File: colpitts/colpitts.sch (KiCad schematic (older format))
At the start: 37 parts, among them J101 BORNERA, J102 BNC, Q101 2N3904, Q102 2N3904, Q103 2N3904, Q104 2N3904, U101 LM741

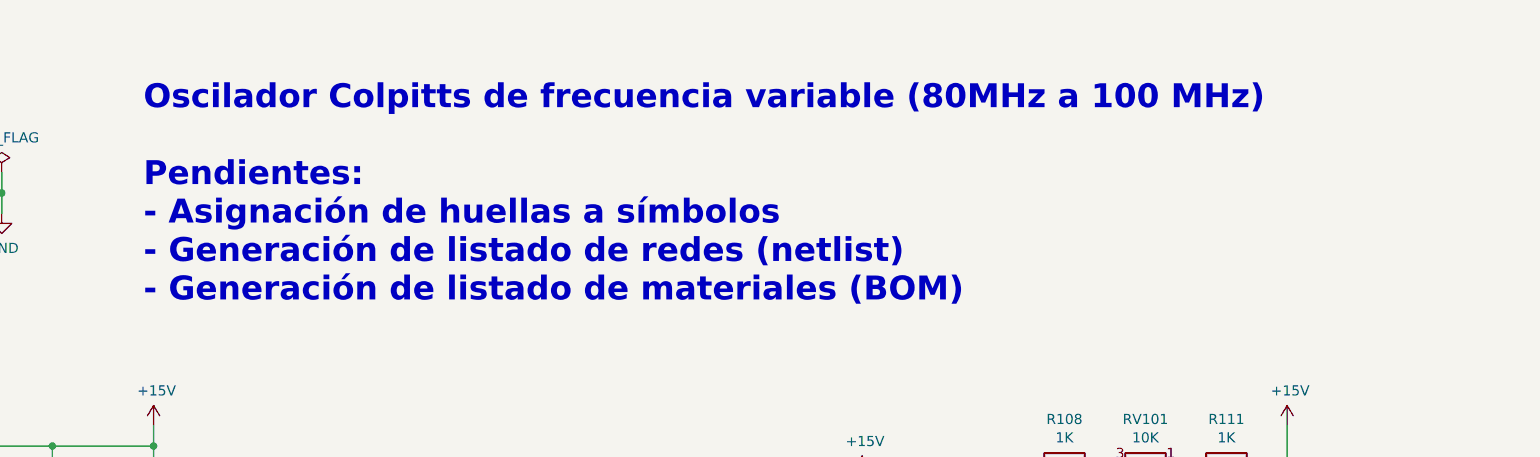
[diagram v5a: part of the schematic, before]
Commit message: Update diseño esquemático (asignación de huellas y modelos 3d)
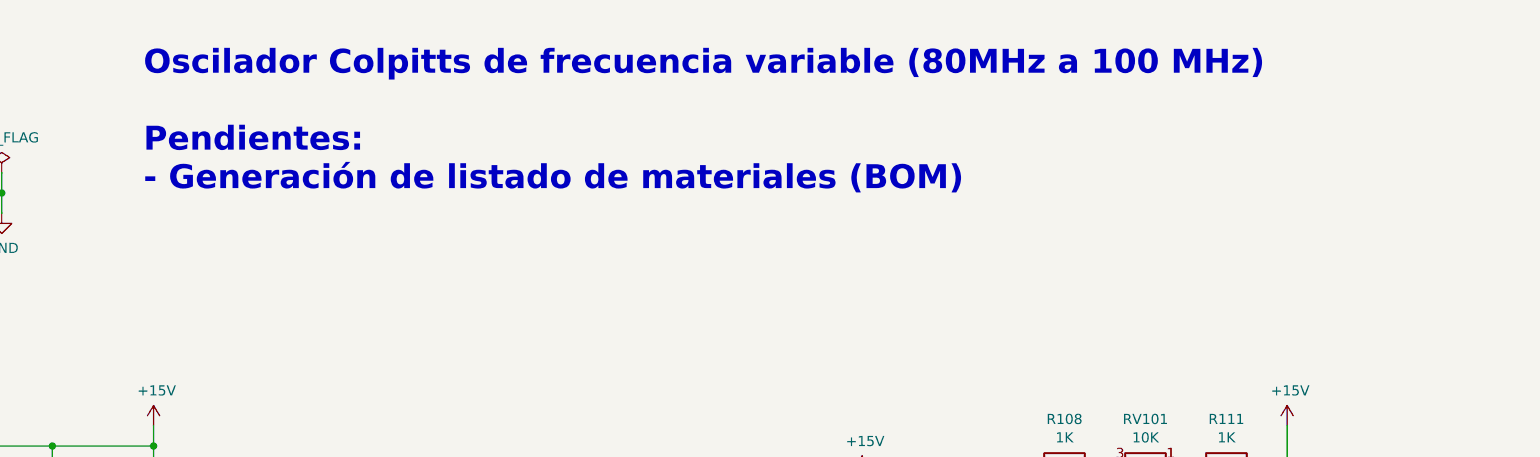
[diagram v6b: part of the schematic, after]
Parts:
- C101, C102, C103, C104, C105, C106, C107, C108, C110, C111, C112, C113, C114, C115: footprint (none) -> Capacitor_SMD:C_0805_2012Metric_Pad1.15x1.40mm_HandSolder
- C109: footprint (none) -> colpitts:Trimmer_Capacitor_Verde
- J101: footprint (none) -> colpitts:TerminalBlock_1x04_P5.00mm
- J102: footprint (none) -> colpitts:BNC_Conn_Horizontal
- JP101, JP102: footprint (none) -> Connector_PinHeader_2.54mm:PinHeader_1x02_P2.54mm_Vertical
- L101: footprint (none) -> Inductor_THT:L_Axial_L5.3mm_D2.2mm_P10.16mm_Horizontal_Vishay_IM-1
- R101, R102, R103, R104, R105, R106, R107, R108, R109, R110, R111: footprint (none) -> Resistor_SMD:R_0805_2012Metric_Pad1.15x1.40mm_HandSolder
- RV101: footprint (none) -> colpitts:Preset_Multivuelta
- U101: footprint (none) -> Package_DIP:DIP-8_W10.16mm
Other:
- note added: "Oscilador Colpitts de frecuencia variable (80MHz a 100 MHz)\n\nPendientes:\n- Generación de listado de materiales (BOM)"
- note removed: "Oscilador Colpitts de frecuencia variable (80MHz a 100 MHz)\n\nPendientes:\n- Asignación de huellas a símbolos\n- Generación de listado de redes (netlist)\n- Generación de listado de materiales (BOM)"
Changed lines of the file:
@@
 F 0 "C101" H 2115 3146 50  0000 L CNN
 F 1 "1nF" H 2115 3055 50  0000 L CNN
-F 2 "" H 2038 2950 50  0001 C CNN
+F 2 "Capacitor_SMD:C_0805_2012Metric_Pad1.15x1.40mm_HandSolder" H 2038 2950 50  0001 C CNN
 F 3 "~" H 2000 3100 50  0001 C CNN
 	1    2000 3100
@@
 F 0 "C103" H 2615 3146 50  0000 L CNN
 F 1 "10nF" H 2615 3055 50  0000 L CNN
-F 2 "" H 2538 2950 50  0001 C CNN
+F 2 "Capacitor_SMD:C_0805_2012Metric_Pad1.15x1.40mm_HandSolder" H 2538 2950 50  0001 C CNN
 F 3 "~" H 2500 3100 50  0001 C CNN
 	1    2500 3100
@@
 F 0 "C105" H 3115 3146 50  0000 L CNN
 F 1 "100nF" H 3115 3055 50  0000 L CNN
-F 2 "" H 3038 2950 50  0001 C CNN
+F 2 "Capacitor_SMD:C_0805_2012Metric_Pad1.15x1.40mm_HandSolder" H 3038 2950 50  0001 C CNN
 F 3 "~" H 3000 3100 50  0001 C CNN
 	1    3000 3100
@@
 F 0 "R102" H 3570 3146 50  0000 L CNN
 F 1 "10K" H 3570 3055 50  0000 L CNN
-F 2 "" V 3430 3100 50  0001 C CNN
+F 2 "Resistor_SMD:R_0805_2012Metric_Pad1.15x1.40mm_HandSolder" V 3430 3100 50  0001 C CNN
 F 3 "~" H 3500 3100 50  0001 C CNN
 	1    3500 3100
@@
 F 0 "L101" H 4053 3146 50  0000 L CNN
 F 1 "40n" H 4053 3055 50  0000 L CNN
-F 2 "" H 4000 3100 50  0001 C CNN
+F 2 "Inductor_THT:L_Axial_L5.3mm_D2.2mm_P10.16mm_Horizontal_Vishay_IM-1" H 4000 3100 50  0001 C CNN
 F 3 "~" H 4000 3100 50  0001 C CNN
 	1    4000 3100
@@
 F 0 "R103" H 3570 4246 50  0000 L CNN
 F 1 "10K" H 3570 4155 50  0000 L CNN
-F 2 "" V 3430 4200 50  0001 C CNN
+F 2 "Resistor_SMD:R_0805_2012Metric_Pad1.15x1.40mm_HandSolder" V 3430 4200 50  0001 C CNN
 F 3 "~" H 3500 4200 50  0001 C CNN
 	1    3500 4200
@@
 F 0 "C102" H 2115 4246 50  0000 L CNN
 F 1 "1nF" H 2115 4155 50  0000 L CNN
-F 2 "" H 2038 4050 50  0001 C CNN
+F 2 "Capacitor_SMD:C_0805_2012Metric_Pad1.15x1.40mm_HandSolder" H 2038 4050 50  0001 C CNN
 F 3 "~" H 2000 4200 50  0001 C CNN
 	1    2000 4200
@@
 F 0 "C104" H 2615 4246 50  0000 L CNN
 F 1 "10nF" H 2615 4155 50  0000 L CNN
-F 2 "" H 2538 4050 50  0001 C CNN
+F 2 "Capacitor_SMD:C_0805_2012Metric_Pad1.15x1.40mm_HandSolder" H 2538 4050 50  0001 C CNN
 F 3 "~" H 2500 4200 50  0001 C CNN
 	1    2500 4200
@@
 F 0 "C106" H 3115 4246 50  0000 L CNN
 F 1 "100nF" H 3115 4155 50  0000 L CNN
-F 2 "" H 3038 4050 50  0001 C CNN
+F 2 "Capacitor_SMD:C_0805_2012Metric_Pad1.15x1.40mm_HandSolder" H 3038 4050 50  0001 C CNN
 F 3 "~" H 3000 4200 50  0001 C CNN
 	1    3000 4200
@@
 F 0 "R105" H 3930 5404 50  0000 R CNN
 F 1 "330" H 3930 5495 50  0000 R CNN
-F 2 "" V 3930 5450 50  0001 C CNN
+F 2 "Resistor_SMD:R_0805_2012Metric_Pad1.15x1.40mm_HandSolder" V 3930 5450 50  0001 C CNN
 F 3 "~" H 4000 5450 50  0001 C CNN
 	1    4000 5450
@@
 F 0 "R104" V 3957 5950 50  0000 C CNN
 F 1 "330" V 3866 5950 50  0000 C CNN
-F 2 "" V 3680 5950 50  0001 C CNN
+F 2 "Resistor_SMD:R_0805_2012Metric_Pad1.15x1.40mm_HandSolder" V 3680 5950 50  0001 C CNN
 F 3 "~" H 3750 5950 50  0001 C CNN
 	1    3750 5950
@@
 F 0 "R101" V 2957 4950 50  0000 C CNN
 F 1 "3.9K" V 2866 4950 50  0000 C CNN
-F 2 "" V 2680 4950 50  0001 C CNN
+F 2 "Resistor_SMD:R_0805_2012Metric_Pad1.15x1.40mm_HandSolder" V 2680 4950 50  0001 C CNN
 F 3 "~" H 2750 4950 50  0001 C CNN
 	1    2750 4950
@@
 F 0 "C107" H 4615 3996 50  0000 L CNN
 F 1 "15pF" H 4615 3905 50  0000 L CNN
-F 2 "" H 4538 3800 50  0001 C CNN
+F 2 "Capacitor_SMD:C_0805_2012Metric_Pad1.15x1.40mm_HandSolder" H 4538 3800 50  0001 C CNN
 F 3 "~" H 4500 3950 50  0001 C CNN
 	1    4500 3950
@@
 F 0 "C108" H 4615 4496 50  0000 L CNN
 F 1 "68pF" H 4615 4405 50  0000 L CNN
-F 2 "" H 4538 4300 50  0001 C CNN
+F 2 "Capacitor_SMD:C_0805_2012Metric_Pad1.15x1.40mm_HandSolder" H 4538 4300 50  0001 C CNN
 F 3 "~" H 4500 4450 50  0001 C CNN
 	1    4500 4450
@@
 F 0 "C109" H 5125 3950 50  0000 L CNN
 F 1 "TRIM VERDE (5.2pF-30pF)" H 4525 4575 50  0000 L CNN
-F 2 "" H 5000 3950 50  0001 C CNN
+F 2 "colpitts:Trimmer_Capacitor_Verde" H 5000 3950 50  0001 C CNN
 F 3 "~" H 5000 3950 50  0001 C CNN
 	1    5000 3950
@@
 F 0 "C110" H 5615 3996 50  0000 L CNN
 F 1 "10pF" H 5615 3905 50  0000 L CNN
-F 2 "" H 5538 3800 50  0001 C CNN
+F 2 "Capacitor_SMD:C_0805_2012Metric_Pad1.15x1.40mm_HandSolder" H 5538 3800 50  0001 C CNN
 F 3 "~" H 5500 3950 50  0001 C CNN
 	1    5500 3950
@@
 F 0 "C111" H 5615 4496 50  0000 L CNN
 F 1 "33pF" H 5615 4405 50  0000 L CNN
-F 2 "" H 5538 4300 50  0001 C CNN
+F 2 "Capacitor_SMD:C_0805_2012Metric_Pad1.15x1.40mm_HandSolder" H 5538 4300 50  0001 C CNN
 F 3 "~" H 5500 4450 50  0001 C CNN
 	1    5500 4450
@@
 F 0 "C112" V 5748 3500 50  0000 C CNN
 F 1 "100nF" V 5839 3500 50  0000 C CNN
-F 2 "" H 6038 3350 50  0001 C CNN
+F 2 "Capacitor_SMD:C_0805_2012Metric_Pad1.15x1.40mm_HandSolder" H 6038 3350 50  0001 C CNN
 F 3 "~" H 6000 3500 50  0001 C CNN
 	1    6000 3500
@@
 F 0 "J102" H 6350 4225 50  0000 L CNN
 F 1 "BNC" H 6350 4134 50  0000 L CNN
-F 2 "" H 6250 4250 50  0001 C CNN
+F 2 "colpitts:BNC_Conn_Horizontal" H 6250 4250 50  0001 C CNN
 F 3 " ~" H 6250 4250 50  0001 C CNN
 	1    6250 4250
@@
 F 0 "JP101" H 2250 5093 50  0000 C CNN
 F 1 "Jumper_2_Open" H 2250 5094 50  0001 C CNN
-F 2 "" H 2250 4950 50  0001 C CNN
+F 2 "Connector_PinHeader_2.54mm:PinHeader_1x02_P2.54mm_Vertical" H 2250 4950 50  0001 C CNN
 F 3 "~" H 2250 4950 50  0001 C CNN
 	1    2250 4950
@@
 F 0 "JP102" H 6500 3643 50  0000 C CNN
 F 1 "Jumper_2_Open" H 6500 3644 50  0001 C CNN
-F 2 "" H 6500 3500 50  0001 C CNN
+F 2 "Connector_PinHeader_2.54mm:PinHeader_1x02_P2.54mm_Vertical" H 6500 3500 50  0001 C CNN
 F 3 "~" H 6500 3500 50  0001 C CNN
 	1    6500 3500
@@
 F 0 "R106" H 6930 4054 50  0000 R CNN
 F 1 "10K" H 6930 4145 50  0000 R CNN
-F 2 "" V 6930 4100 50  0001 C CNN
+F 2 "Resistor_SMD:R_0805_2012Metric_Pad1.15x1.40mm_HandSolder" V 6930 4100 50  0001 C CNN
 F 3 "~" H 7000 4100 50  0001 C CNN
 	1    7000 4100
@@
 F 0 "R107" H 7430 4054 50  0000 R CNN
 F 1 "5.6K" H 7430 4145 50  0000 R CNN
-F 2 "" V 7430 4100 50  0001 C CNN
+F 2 "Resistor_SMD:R_0805_2012Metric_Pad1.15x1.40mm_HandSolder" V 7430 4100 50  0001 C CNN
 F 3 "~" H 7500 4100 50  0001 C CNN
 	1    7500 4100
@@
 F 0 "C114" H 8725 4050 50  0000 C CNN
 F 1 "100pF" H 8650 4150 50  0000 C CNN
-F 2 "" H 8938 3950 50  0001 C CNN
+F 2 "Capacitor_SMD:C_0805_2012Metric_Pad1.15x1.40mm_HandSolder" H 8938 3950 50  0001 C CNN
 F 3 "~" H 8900 4100 50  0001 C CNN
 	1    8900 4100
@@
 F 0 "R110" H 8830 4454 50  0000 R CNN
 F 1 "1K" H 8830 4545 50  0000 R CNN
-F 2 "" V 8830 4500 50  0001 C CNN
+F 2 "Resistor_SMD:R_0805_2012Metric_Pad1.15x1.40mm_HandSolder" V 8830 4500 50  0001 C CNN
 F 3 "~" H 8900 4500 50  0001 C CNN
 	1    8900 4500
@@
 F 0 "RV101" V 8693 2925 50  0000 C CNN
 F 1 "10K" V 8784 2925 50  0000 C CNN
-F 2 "" H 8900 2925 50  0001 C CNN
+F 2 "colpitts:Preset_Multivuelta" H 8900 2925 50  0001 C CNN
 F 3 "~" H 8900 2925 50  0001 C CNN
 	1    8900 2925
@@
 F 0 "U101" H 9650 4000 50  0000 L CNN
 F 1 "LM741" H 9650 3900 50  0000 L CNN
-F 2 "" H 9750 3750 50  0001 C CNN
+F 2 "Package_DIP:DIP-8_W10.16mm" H 9750 3750 50  0001 C CNN
 F 3 "http://www.ti.com/lit/ds/symlink/lm741.pdf" H 9850 3850 50  0001 C CNN
 	1    9700 3700
@@
 F 0 "R108" V 8707 2925 50  0000 C CNN
 F 1 "1K" V 8616 2925 50  0000 C CNN
-F 2 "" V 8430 2925 50  0001 C CNN
+F 2 "Resistor_SMD:R_0805_2012Metric_Pad1.15x1.40mm_HandSolder" V 8430 2925 50  0001 C CNN
 F 3 "~" H 8500 2925 50  0001 C CNN
 	1    8500 2925
@@
 F 0 "R111" V 9507 2925 50  0000 C CNN
 F 1 "1K" V 9416 2925 50  0000 C CNN
-F 2 "" V 9230 2925 50  0001 C CNN
+F 2 "Resistor_SMD:R_0805_2012Metric_Pad1.15x1.40mm_HandSolder" V 9230 2925 50  0001 C CNN
 F 3 "~" H 9300 2925 50  0001 C CNN
 	1    9300 2925
@@
 F 0 "R109" V 8707 3800 50  0000 C CNN
 F 1 "1K" V 8616 3800 50  0000 C CNN
-F 2 "" V 8430 3800 50  0001 C CNN
+F 2 "Resistor_SMD:R_0805_2012Metric_Pad1.15x1.40mm_HandSolder" V 8430 3800 50  0001 C CNN
 F 3 "~" H 8500 3800 50  0001 C CNN
 	1    8500 3800
@@
 F 0 "C115" H 10215 3196 50  0000 L CNN
 F 1 "100nF" H 10215 3105 50  0000 L CNN
-F 2 "" H 10138 3000 50  0001 C CNN
+F 2 "Capacitor_SMD:C_0805_2012Metric_Pad1.15x1.40mm_HandSolder" H 10138 3000 50  0001 C CNN
 F 3 "~" H 10100 3150 50  0001 C CNN
 	1    10100 3150
@@
 F 0 "C113" H 7825 4050 50  0000 C CNN
 F 1 "10nF" H 7800 4150 50  0000 C CNN
-F 2 "" H 8038 3950 50  0001 C CNN
+F 2 "Capacitor_SMD:C_0805_2012Metric_Pad1.15x1.40mm_HandSolder" H 8038 3950 50  0001 C CNN
 F 3 "~" H 8000 4100 50  0001 C CNN
 	1    8000 4100
@@
 F 0 "J101" H 2450 1150 50  0000 C CNN
 F 1 "BORNERA" H 2450 1250 50  0000 C CNN
-F 2 "" H 2500 1600 50  0001 C CNN
+F 2 "colpitts:TerminalBlock_1x04_P5.00mm" H 2500 1600 50  0001 C CNN
 F 3 "~" H 2500 1600 50  0001 C CNN
 	1    2500 1600
@@
 	3250 1600 3250 1500
 Connection ~ 3250 1600
-Text Notes 3950 2150 0    118  ~ 24
-Oscilador Colpitts de frecuencia variable (80MHz a 100 MHz)\n\nPendientes:\n- Asignación de huellas a símbolos\n- Generación de listado de redes (netlist)\n- Generación de listado de materiales (BOM)
+Text Notes 3950 1600 0    118  ~ 24
+Oscilador Colpitts de frecuencia variable (80MHz a 100 MHz)\n\nPendientes:\n- Generación de listado de materiales (BOM)
 Text Label 1500 4950 0    50   ~ 0
 Vcontrol

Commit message: Fin diseño esquemático (bom generada)
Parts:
- C109: Description (none) -> CAP TRIMMER 5.2-30PF 100V TH; DigiKey PN (none) -> 490-1960-ND; Manf PN (none) -> TZ03R300E169B00
- J101: Description (none) -> TERM BLK 4POS SIDE ENTRY 5MM PCB; DigiKey PN (none) -> 277-1579-ND; Manf PN (none) -> 1935187
- J102: Description (none) -> CONN BNC JACK R/A 50 OHM PCB; DigiKey PN (none) -> A32244-ND; Manf PN (none) -> 5227161-1
- Q101, Q102, Q103, Q104: Description (none) -> TRANS NPN 40V 0.2A TO-92; DigiKey PN (none) -> 2N3904FS-ND; Manf PN (none) -> 2N3904BU
- U101: Description (none) -> IC OPAMP GP 1 CIRCUIT 8DIP; DigiKey PN (none) -> LM741CNNS/NOPB-ND; Manf PN (none) -> LM741CN/NOPB
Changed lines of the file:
@@
 F 1 "2N3904" H 4090 3905 50  0000 L CNN
 F 2 "Package_TO_SOT_THT:TO-92_Inline" H 4100 3875 50  0001 L CIN
-F 3 "https://www.fairchildsemi.com/datasheets/2N/2N3904.pdf" H 3900 3950 50  0001 L CNN
+F 3 "https://www.onsemi.com/pub/Collateral/PZT3904-D.pdf" H 3900 3950 50  0001 L CNN
+F 4 "TRANS NPN 40V 0.2A TO-92" H 3900 3950 50  0001 C CNN "Description"
+F 5 "2N3904FS-ND" H 3900 3950 50  0001 C CNN "DigiKey PN"
+F 6 "2N3904BU" H 3900 3950 50  0001 C CNN "Manf PN"
 	1    3900 3950
 	1    0    0    -1
@@
 F 1 "2N3904" H 4090 4905 50  0000 L CNN
 F 2 "Package_TO_SOT_THT:TO-92_Inline" H 4100 4875 50  0001 L CIN
-F 3 "https://www.fairchildsemi.com/datasheets/2N/2N3904.pdf" H 3900 4950 50  0001 L CNN
+F 3 "https://www.onsemi.com/pub/Collateral/PZT3904-D.pdf" H 3900 4950 50  0001 L CNN
+F 4 "TRANS NPN 40V 0.2A TO-92" H 3900 4950 50  0001 C CNN "Description"
+F 5 "2N3904FS-ND" H 3900 4950 50  0001 C CNN "DigiKey PN"
+F 6 "2N3904BU" H 3900 4950 50  0001 C CNN "Manf PN"
 	1    3900 4950
 	1    0    0    -1
@@
 F 1 "2N3904" H 3590 5405 50  0000 L CNN
 F 2 "Package_TO_SOT_THT:TO-92_Inline" H 3600 5375 50  0001 L CIN
-F 3 "https://www.fairchildsemi.com/datasheets/2N/2N3904.pdf" H 3400 5450 50  0001 L CNN
+F 3 "https://www.onsemi.com/pub/Collateral/PZT3904-D.pdf" H 3400 5450 50  0001 L CNN
+F 4 "TRANS NPN 40V 0.2A TO-92" H 3400 5450 50  0001 C CNN "Description"
+F 5 "2N3904FS-ND" H 3400 5450 50  0001 C CNN "DigiKey PN"
+F 6 "2N3904BU" H 3400 5450 50  0001 C CNN "Manf PN"
 	1    3400 5450
 	1    0    0    -1
@@
 F 1 "TRIM VERDE (5.2pF-30pF)" H 4525 4575 50  0000 L CNN
 F 2 "colpitts:Trimmer_Capacitor_Verde" H 5000 3950 50  0001 C CNN
-F 3 "~" H 5000 3950 50  0001 C CNN
+F 3 "https://media.digikey.com/pdf/Data%20Sheets/Murata%20PDFs/Ceramic_Trimmer_Cap_Cat.pdf#page=34" H 5000 3950 50  0001 C CNN
+F 4 "CAP TRIMMER 5.2-30PF 100V TH" H 5000 3950 50  0001 C CNN "Description"
+F 5 "490-1960-ND" H 5000 3950 50  0001 C CNN "DigiKey PN"
+F 6 "TZ03R300E169B00" H 5000 3950 50  0001 C CNN "Manf PN"
 	1    5000 3950
 	1    0    0    -1
@@
 F 1 "BNC" H 6350 4134 50  0000 L CNN
 F 2 "colpitts:BNC_Conn_Horizontal" H 6250 4250 50  0001 C CNN
-F 3 " ~" H 6250 4250 50  0001 C CNN
+F 3 "https://www.te.com/commerce/DocumentDelivery/DDEController?Action=srchrtrv&DocNm=5227161&DocType=Customer+Drawing&DocLang=English" H 6250 4250 50  0001 C CNN
+F 4 "CONN BNC JACK R/A 50 OHM PCB" H 6250 4250 50  0001 C CNN "Description"
+F 5 "A32244-ND" H 6250 4250 50  0001 C CNN "DigiKey PN"
+F 6 "5227161-1" H 6250 4250 50  0001 C CNN "Manf PN"
 	1    6250 4250
 	1    0    0    -1
@@
 F 1 "2N3904" H 7590 3455 50  0000 L CNN
 F 2 "Package_TO_SOT_THT:TO-92_Inline" H 7600 3425 50  0001 L CIN
-F 3 "https://www.fairchildsemi.com/datasheets/2N/2N3904.pdf" H 7400 3500 50  0001 L CNN
+F 3 "https://www.onsemi.com/pub/Collateral/PZT3904-D.pdf" H 7400 3500 50  0001 L CNN
+F 4 "TRANS NPN 40V 0.2A TO-92" H 7400 3500 50  0001 C CNN "Description"
+F 5 "2N3904FS-ND" H 7400 3500 50  0001 C CNN "DigiKey PN"
+F 6 "2N3904BU" H 7400 3500 50  0001 C CNN "Manf PN"
 	1    7400 3500
 	1    0    0    -1
@@
 F 2 "Package_DIP:DIP-8_W10.16mm" H 9750 3750 50  0001 C CNN
 F 3 "http://www.ti.com/lit/ds/symlink/lm741.pdf" H 9850 3850 50  0001 C CNN
+F 4 "IC OPAMP GP 1 CIRCUIT 8DIP" H 9700 3700 50  0001 C CNN "Description"
+F 5 "LM741CNNS/NOPB-ND" H 9700 3700 50  0001 C CNN "DigiKey PN"
+F 6 "LM741CN/NOPB" H 9700 3700 50  0001 C CNN "Manf PN"
 	1    9700 3700
 	1    0    0    -1
@@
 F 1 "BORNERA" H 2450 1250 50  0000 C CNN
 F 2 "colpitts:TerminalBlock_1x04_P5.00mm" H 2500 1600 50  0001 C CNN
-F 3 "~" H 2500 1600 50  0001 C CNN
+F 3 "https://media.digikey.com/pdf/Data%20Sheets/Phoenix%20Contact%20PDFs/1935187.pdf" H 2500 1600 50  0001 C CNN
+F 4 "TERM BLK 4POS SIDE ENTRY 5MM PCB" H 2500 1600 50  0001 C CNN "Description"
+F 5 "277-1579-ND" H 2500 1600 50  0001 C CNN "DigiKey PN"
+F 6 "1935187" H 2500 1600 50  0001 C CNN "Manf PN"
 	1    2500 1600
 	-1   0    0    1

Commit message: Lectura de netlist, def área pcb, board setup
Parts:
- added FID101, FID102, FID103, FID104, FID105, FID106: Fiducial, Fiducial:Fiducial_1mm_Mask2mm, symbol Mechanical:Fiducial
- added H101, H102, H103, H104: MountingHole, MountingHole:MountingHole_3.2mm_M3_Pad_Via, symbol Mechanical:MountingHole
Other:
- note added: "Oscilador Colpitts de frecuencia variable (80MHz a 100 MHz)"
- note removed: "Oscilador Colpitts de frecuencia variable (80MHz a 100 MHz)\n\nPendientes:\n- Generación de listado de materiales (BOM)"
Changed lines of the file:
@@
 	3250 1600 3250 1500
 Connection ~ 3250 1600
-Text Notes 3950 1600 0    118  ~ 24
-Oscilador Colpitts de frecuencia variable (80MHz a 100 MHz)\n\nPendientes:\n- Generación de listado de materiales (BOM)
 Text Label 1500 4950 0    50   ~ 0
 Vcontrol
+$Comp
+L Mechanical:MountingHole H102
+U 1 1 5D64AAE2
+P 2200 6750
+F 0 "H102" H 2300 6796 50  0000 L CNN
+F 1 "MountingHole" H 2300 6705 50  0000 L CNN
+F 2 "MountingHole:MountingHole_3.2mm_M3_Pad_Via" H 2200 6750 50  0001 C CNN
+F 3 "~" H 2200 6750 50  0001 C CNN
+	1    2200 6750
+	1    0    0    -1
+$EndComp
+$Comp
+L Mechanical:MountingHole H103
+U 1 1 5D64BDE5
+P 2200 7000
+F 0 "H103" H 2300 7046 50  0000 L CNN
+F 1 "MountingHole" H 2300 6955 50  0000 L CNN
+F 2 "MountingHole:MountingHole_3.2mm_M3_Pad_Via" H 2200 7000 50  0001 C CNN
+F 3 "~" H 2200 7000 50  0001 C CNN
+	1    2200 7000
+	1    0    0    -1
+$EndComp
+$Comp
+L Mechanical:MountingHole H104
+U 1 1 5D64C1E4
+P 2200 7250
+F 0 "H104" H 2300 7296 50  0000 L CNN
+F 1 "MountingHole" H 2300 7205 50  0000 L CNN
+F 2 "MountingHole:MountingHole_3.2mm_M3_Pad_Via" H 2200 7250 50  0001 C CNN
+F 3 "~" H 2200 7250 50  0001 C CNN
+	1    2200 7250
+	1    0    0    -1
+$EndComp
+$Comp
+L Mechanical:Fiducial FID101
+U 1 1 5D64C73B
+P 3000 6500
+F 0 "FID101" H 3085 6546 50  0000 L CNN
+F 1 "Fiducial" H 3085 6455 50  0000 L CNN
+F 2 "Fiducial:Fiducial_1mm_Mask2mm" H 3000 6500 50  0001 C CNN
+F 3 "~" H 3000 6500 50  0001 C CNN
+	1    3000 6500
+	1    0    0    -1
+$EndComp
+$Comp
+L Mechanical:Fiducial FID102
+U 1 1 5D64D3CD
+P 3000 6750
+F 0 "FID102" H 3085 6796 50  0000 L CNN
+F 1 "Fiducial" H 3085 6705 50  0000 L CNN
+F 2 "Fiducial:Fiducial_1mm_Mask2mm" H 3000 6750 50  0001 C CNN
+F 3 "~" H 3000 6750 50  0001 C CNN
+	1    3000 6750
+	1    0    0    -1
+$EndComp
+$Comp
+L Mechanical:Fiducial FID103
+U 1 1 5D64DC22
+P 3000 7000
+F 0 "FID103" H 3085 7046 50  0000 L CNN
+F 1 "Fiducial" H 3085 6955 50  0000 L CNN
+F 2 "Fiducial:Fiducial_1mm_Mask2mm" H 3000 7000 50  0001 C CNN
+F 3 "~" H 3000 7000 50  0001 C CNN
+	1    3000 7000
+	1    0    0    -1
+$EndComp
+$Comp
+L Mechanical:Fiducial FID105
+U 1 1 5D64E59B
+P 3500 6750
+F 0 "FID105" H 3585 6796 50  0000 L CNN
+F 1 "Fiducial" H 3585 6705 50  0000 L CNN
+F 2 "Fiducial:Fiducial_1mm_Mask2mm" H 3500 6750 50  0001 C CNN
+F 3 "~" H 3500 6750 50  0001 C CNN
+	1    3500 6750
+	1    0    0    -1
+$EndComp
+$Comp
+L Mechanical:Fiducial FID106
+U 1 1 5D64E82A
+P 3500 7000
+F 0 "FID106" H 3585 7046 50  0000 L CNN
+F 1 "Fiducial" H 3585 6955 50  0000 L CNN
+F 2 "Fiducial:Fiducial_1mm_Mask2mm" H 3500 7000 50  0001 C CNN
+F 3 "~" H 3500 7000 50  0001 C CNN
+	1    3500 7000
+	1    0    0    -1
+$EndComp
+Text Notes 3950 2100 0    118  ~ 24
+Oscilador Colpitts de frecuencia variable (80MHz a 100 MHz)
+$Comp
+L Mechanical:MountingHole H101
+U 1 1 5D64C32C
+P 2200 6500
+F 0 "H101" H 2300 6546 50  0000 L CNN
+F 1 "MountingHole" H 2300 6455 50  0000 L CNN
+F 2 "MountingHole:MountingHole_3.2mm_M3_Pad_Via" H 2200 6500 50  0001 C CNN
+F 3 "~" H 2200 6500 50  0001 C CNN
+	1    2200 6500
+	1    0    0    -1
+$EndComp
+$Comp
+L Mechanical:Fiducial FID104
+U 1 1 5D64E2FA
+P 3500 6500
+F 0 "FID104" H 3585 6546 50  0000 L CNN
+F 1 "Fiducial" H 3585 6455 50  0000 L CNN
+F 2 "Fiducial:Fiducial_1mm_Mask2mm" H 3500 6500 50  0001 C CNN
+F 3 "~" H 3500 6500 50  0001 C CNN
+	1    3500 6500
+	1    0    0    -1
+$EndComp
 $EndSCHEMATC
